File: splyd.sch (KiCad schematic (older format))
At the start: 262 parts

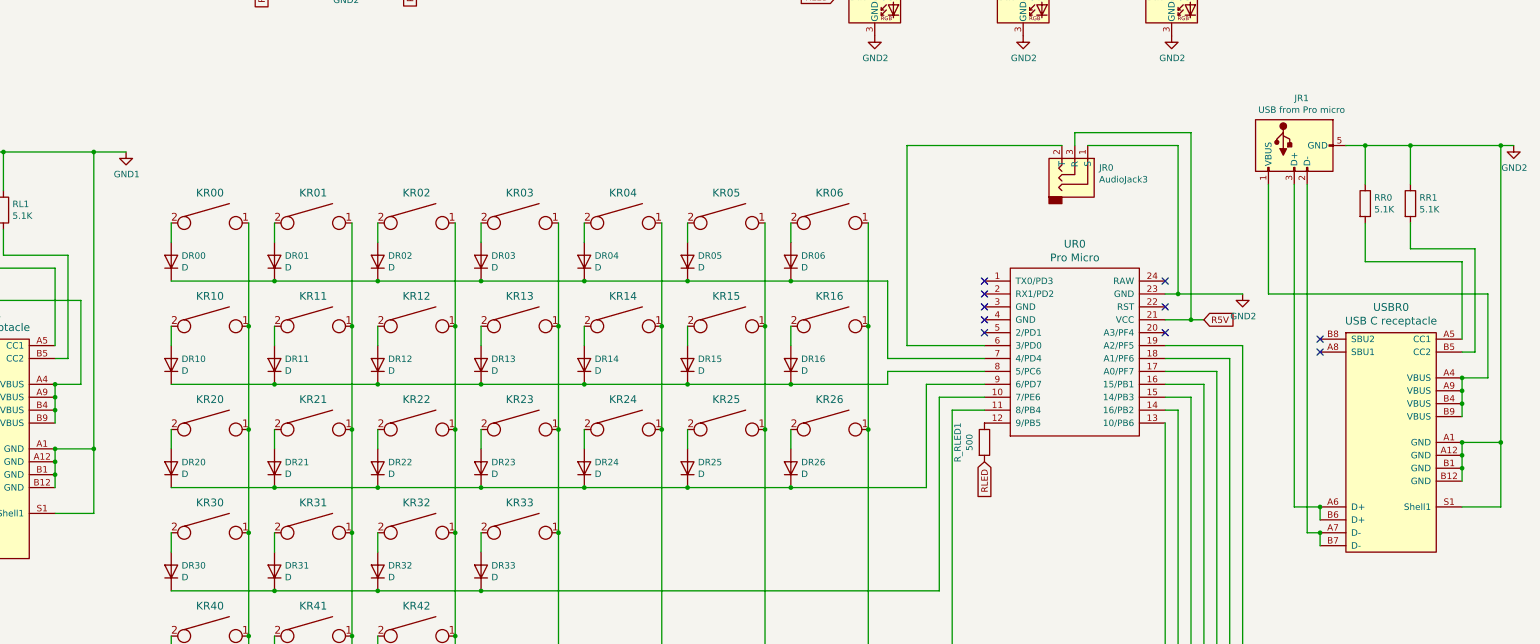
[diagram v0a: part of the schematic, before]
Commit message: Edge cut rework and prep for case design
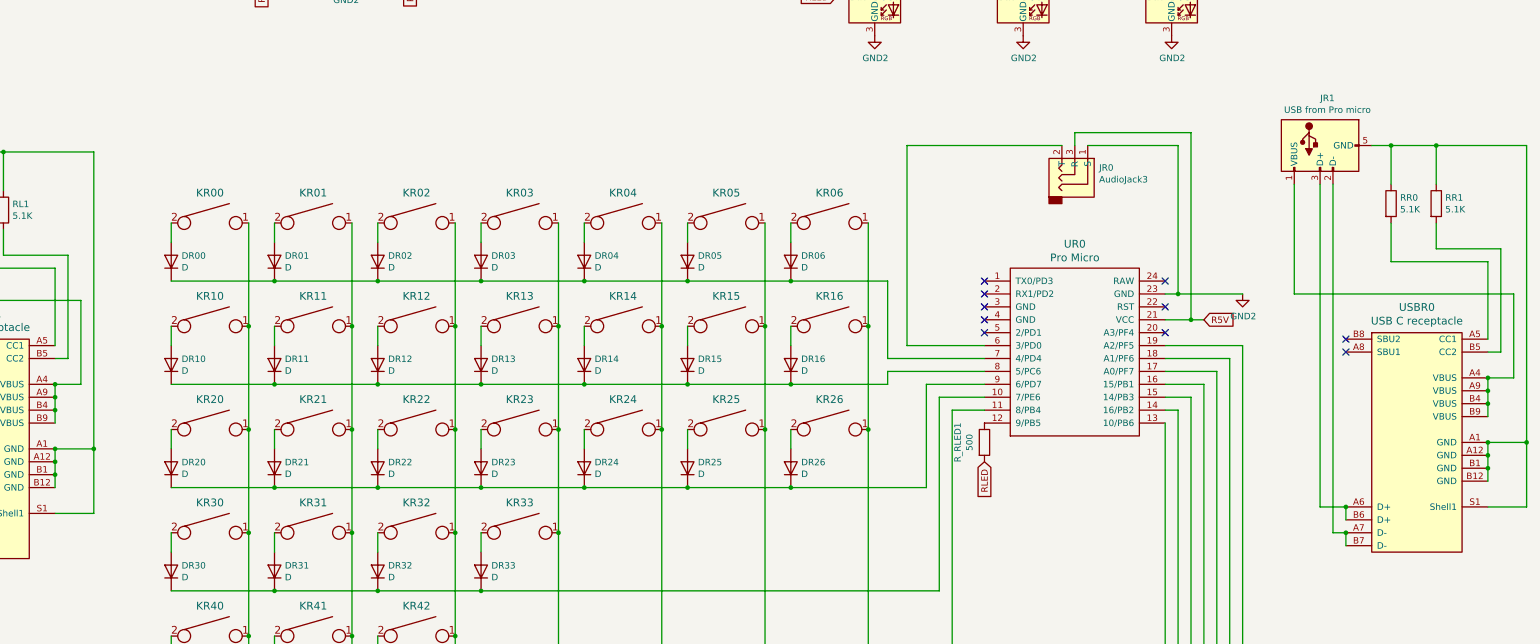
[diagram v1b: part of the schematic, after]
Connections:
- net GND1: no longer JL1.5 (GND), RL0.1, RL1.1, USBL1.A1 (GND), USBL1.A12 (GND), USBL1.B1 (GND), USBL1.B12 (GND), USBL1.S1 (Shell1)
- net GND2: no longer JR1.5 (GND), RR0.1, RR1.1, USBR0.A1 (GND), USBR0.A12 (GND), USBR0.B1 (GND), USBR0.B12 (GND), USBR0.S1 (Shell1)
- new net: JL1.5 (GND), RL0.1, RL1.1, USBL1.A1 (GND), USBL1.A12 (GND), USBL1.B1 (GND), USBL1.B12 (GND), USBL1.S1 (Shell1)
- new net: JR1.5 (GND), RR0.1, RR1.1, USBR0.A1 (GND), USBR0.A12 (GND), USBR0.B1 (GND), USBR0.B12 (GND), USBR0.S1 (Shell1)
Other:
- moved on the sheet: JR1, RR0, RR1, USBR0
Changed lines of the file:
@@
 L Device:R RR1
 U 1 1 5F7A600E
-P 21800 9800
-F 0 "RR1" H 21870 9846 50  0000 L CNN
-F 1 "5.1K" H 21870 9755 50  0000 L CNN
-F 2 "Resistor_SMD:R_0603_1608Metric" V 21730 9800 50  0001 C CNN
-F 3 "~" H 21800 9800 50  0001 C CNN
-	1    21800 9800
+P 22000 9800
+F 0 "RR1" H 22070 9846 50  0000 L CNN
+F 1 "5.1K" H 22070 9755 50  0000 L CNN
+F 2 "Resistor_SMD:R_0603_1608Metric" V 21930 9800 50  0001 C CNN
+F 3 "~" H 22000 9800 50  0001 C CNN
+	1    22000 9800
 	1    0    0    -1
 $EndComp
@@
 L Device:R RR0
 U 1 1 5F7A6008
-P 21450 9800
-F 0 "RR0" H 21520 9846 50  0000 L CNN
-F 1 "5.1K" H 21520 9755 50  0000 L CNN
-F 2 "Resistor_SMD:R_0603_1608Metric" V 21380 9800 50  0001 C CNN
-F 3 "~" H 21450 9800 50  0001 C CNN
-	1    21450 9800
+P 21650 9800
+F 0 "RR0" H 21720 9846 50  0000 L CNN
+F 1 "5.1K" H 21720 9755 50  0000 L CNN
+F 2 "Resistor_SMD:R_0603_1608Metric" V 21580 9800 50  0001 C CNN
+F 3 "~" H 21650 9800 50  0001 C CNN
+	1    21650 9800
 	1    0    0    -1
 $EndComp
@@
 L Connector:Micro_USB_wires JR1
 U 1 1 5F7A6002
-P 20900 9350
-F 0 "JR1" V 20533 9293 50  0000 C CNN
-F 1 "USB from Pro micro" V 20624 9293 50  0000 C CNN
-F 2 "Connector_Wire:Pad_1x04_SMD_1x2mm" H 21050 9300 50  0001 C CNN
-F 3 "~" H 21050 9300 50  0001 C CNN
-	1    20900 9350
+P 21100 9350
+F 0 "JR1" V 20733 9293 50  0000 C CNN
+F 1 "USB from Pro micro" V 20824 9293 50  0000 C CNN
+F 2 "Connector_Wire:Pad_1x04_SMD_1x2mm" H 21250 9300 50  0001 C CNN
+F 3 "~" H 21250 9300 50  0001 C CNN
+	1    21100 9350
 	0    -1   1    0
 $EndComp
 Wire Wire Line
-	21100 12450 21100 12350
+	21300 12450 21300 12350
 Wire Wire Line
-	21100 12250 21100 12150
+	21300 12250 21300 12150
 Wire Wire Line
-	21100 12150 20900 12150
+	21300 12150 21100 12150
 Wire Wire Line
-	20900 12150 20900 9650
+	21100 12150 21100 9650
 Wire Wire Line
-	21100 12350 21000 12350
+	21300 12350 21200 12350
 Wire Wire Line
-	21000 12350 21000 9650
-NoConn ~ 21100 10950
+	21200 12350 21200 9650
+NoConn ~ 21300 10950
 $Comp
 L keebio:ProMicro UR0
@@
 L Type-C:USB_C_GCT_USB4085 USBR0
 U 1 1 5F7A5FEF
-P 21650 11700
-F 0 "USBR0" H 21650 12797 60  0000 C CNN
-F 1 "USB C receptacle" H 21650 12691 60  0000 C CNN
-F 2 "Type-C:USB_C_GCT_USB4085" H 20950 11750 60  0001 C CNN
-F 3 "" H 20950 11750 60  0001 C CNN
-	1    21650 11700
+P 21850 11700
+F 0 "USBR0" H 21850 12797 60  0000 C CNN
+F 1 "USB C receptacle" H 21850 12691 60  0000 C CNN
+F 2 "Type-C:USB_C_GCT_USB4085" H 21150 11750 60  0001 C CNN
+F 3 "" H 21150 11750 60  0001 C CNN
+	1    21850 11700
 	1    0    0    -1
 $EndComp
-Connection ~ 21100 12150
-Connection ~ 21100 12350
-NoConn ~ 21100 10850
+Connection ~ 21300 12150
+Connection ~ 21300 12350
+NoConn ~ 21300 10850
 Wire Wire Line
-	22200 10850 22200 10250
+	22400 10850 22400 10250
 Wire Wire Line
-	22200 10250 21450 10250
+	22400 10250 21650 10250
 Wire Wire Line
-	21450 10250 21450 9950
+	21650 10250 21650 9950
 Wire Wire Line
-	22200 10950 22300 10950
+	22400 10950 22500 10950
 Wire Wire Line
-	22300 10950 22300 10150
+	22500 10950 22500 10150
 Wire Wire Line
-	22300 10150 21800 10150
+	22500 10150 22000 10150
 Wire Wire Line
-	21800 10150 21800 9950
+	22000 10150 22000 9950
 Wire Wire Line
-	22200 11450 22200 11350
-Connection ~ 22200 11250
+	22400 11450 22400 11350
+Connection ~ 22400 11250
 Wire Wire Line
-	22200 11250 22200 11150
-Connection ~ 22200 11350
+	22400 11250 22400 11150
+Connection ~ 22400 11350
 Wire Wire Line
-	22200 11350 22200 11250
+	22400 11350 22400 11250
 Wire Wire Line
-	22200 11150 22400 11150
+	22400 11150 22600 11150
 Wire Wire Line
-	22400 11150 22400 10500
+	22600 11150 22600 10500
 Wire Wire Line
-	22400 10500 20700 10500
+	22600 10500 20900 10500
 Wire Wire Line
-	20700 10500 20700 9650
-Connection ~ 22200 11150
+	20900 10500 20900 9650
+Connection ~ 22400 11150
 Wire Wire Line
-	22200 11950 22200 11850
-Connection ~ 22200 11750
+	22400 11950 22400 11850
+Connection ~ 22400 11750
 Wire Wire Line
-	22200 11750 22200 11650
-Connection ~ 22200 11850
+	22400 11750 22400 11650
+Connection ~ 22400 11850
 Wire Wire Line
-	22200 11850 22200 11750
+	22400 11850 22400 11750
 Wire Wire Line
-	22200 11650 22500 11650
+	22400 11650 22700 11650
 Wire Wire Line
-	22500 11650 22500 9350
+	22700 11650 22700 9350
 Wire Wire Line
-	22500 9350 21800 9350
-Connection ~ 22200 11650
+	22700 9350 22000 9350
+Connection ~ 22400 11650
 Wire Wire Line
-	21450 9650 21450 9350
-Connection ~ 21450 9350
+	21650 9650 21650 9350
+Connection ~ 21650 9350
 Wire Wire Line
-	21450 9350 21300 9350
+	21650 9350 21500 9350
 Wire Wire Line
-	21800 9650 21800 9350
-Connection ~ 21800 9350
+	22000 9650 22000 9350
+Connection ~ 22000 9350
 Wire Wire Line
-	21800 9350 21450 9350
+	22000 9350 21650 9350
 Wire Wire Line
-	22200 12150 22500 12150
+	22400 12150 22700 12150
 Wire Wire Line
-	22500 12150 22500 11650
-Connection ~ 22500 11650
+	22700 12150 22700 11650
+Connection ~ 22700 11650
 Wire Wire Line
 	14400 9950 14400 10750
@@
 	18250 11400 18250 13600
 NoConn ~ 18500 10400
-Wire Wire Line
-	11600 9400 11850 9400
-Connection ~ 11600 9400
-$Comp
-L power:GND1 #PWR0241
-U 1 1 643BE796
-P 11850 9400
-F 0 "#PWR0241" H 11850 9150 50  0001 C CNN
-F 1 "GND1" H 11855 9227 50  0000 C CNN
-F 2 "" H 11850 9400 50  0001 C CNN
-F 3 "" H 11850 9400 50  0001 C CNN
-	1    11850 9400
-	1    0    0    -1
-$EndComp
-$Comp
-L power:GND2 #PWR0242
-U 1 1 643C109B
-P 22600 9350
-F 0 "#PWR0242" H 22600 9100 50  0001 C CNN
-F 1 "GND2" H 22605 9177 50  0000 C CNN
-F 2 "" H 22600 9350 50  0001 C CNN
-F 3 "" H 22600 9350 50  0001 C CNN
-	1    22600 9350
-	1    0    0    -1
-$EndComp
-Wire Wire Line
-	22500 9350 22600 9350
-Connection ~ 22500 9350
 $EndSCHEMATC
